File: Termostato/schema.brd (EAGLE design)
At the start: 100 x 80 mm, 5 parts, among them K1 RELAY-SPDT-JZC-11F

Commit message: Updated schematics V1.1
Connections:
- new net 3.3V: B1.3.3V, U$1.B2, U$1.D2
- net RX: now also B1.D2; no longer B1.D3
- net TX: now also B1.D3; no longer B1.D2
- net VCC: no longer U$1.D2
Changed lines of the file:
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@@
 <contactref element="B1" pad="VIN"/>
 <contactref element="U1" pad="VDD"/>
-<contactref element="U$1" pad="D2"/>
-<wire x1="72.39" y1="64.77" x2="85.09" y2="41.91" width="0" layer="19" extent="1-1"/>
 <wire x1="55.88" y1="6.35" x2="85.09" y2="41.91" width="0" layer="19" extent="1-1"/>
 </signal>
@@
 <signal name="TX">
 <contactref element="U$1" pad="A2"/>
-<contactref element="B1" pad="D2"/>
-<wire x1="72.39" y1="72.39" x2="68.58" y2="54.61" width="0" layer="19" extent="1-1"/>
+<contactref element="B1" pad="D3"/>
+<wire x1="72.39" y1="72.39" x2="66.04" y2="54.61" width="0" layer="19" extent="1-1"/>
 </signal>
 <signal name="RX">
 <contactref element="U$1" pad="D1"/>
-<contactref element="B1" pad="D3"/>
-<wire x1="74.93" y1="64.77" x2="66.04" y2="54.61" width="0" layer="19" extent="1-1"/>
+<contactref element="B1" pad="D2"/>
+<wire x1="68.58" y1="54.61" x2="74.93" y2="64.77" width="0" layer="19" extent="1-1"/>
+</signal>
+<signal name="3.3V">
+<contactref element="U$1" pad="D2"/>
+<contactref element="B1" pad="3.3V"/>
+<contactref element="U$1" pad="B2"/>
+<wire x1="72.39" y1="64.77" x2="72.39" y2="69.85" width="0" layer="19" extent="1-1"/>
+<wire x1="45.72" y1="6.35" x2="72.39" y2="64.77" width="0" layer="19" extent="1-1"/>
 </signal>
 </signals>

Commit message: Updated schematic
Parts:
- added LCD1: LCD-16X2SILK, SparkFun-Displays:LCD-16X2
- added R1, R2: 220, SparkFun-Resistors:0603
- added S2, S3: (no value), SparkFun-Retired:TACTILE-PTH
- added VR1: 10k, SparkFun-Resistors:TRIMPOT-SMD-TC33X
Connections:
- new net D10: B1.D10, LCD1.12
- new net D11: B1.D11, LCD1.13
- new net D12: B1.D12, LCD1.14
- new net D13: B1.D13, K1.1
- new net D4: B1.D4, S2.4
- new net D5: B1.D5, S3.4
- new net D8: B1.D8, LCD1.6
- new net D9: B1.D9, LCD1.11
- new net N$1: LCD1.3, VR1.2
- new net N$2: R2.1, S2.3
- new net N$4: R1.1, S3.3
- new net N$5: S3.1
- net D7: now also LCD1.4; no longer K1.1
- net GND: now also LCD1.16, LCD1.2, LCD1.5, R1.2, R2.2, VR1.3
- net VCC: now also LCD1.1, LCD1.15, S2.1, VR1.1
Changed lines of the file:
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@@
 <attribute name="PROD_ID" value="SEN-10167" x="88.9" y="41.91" size="1.778" layer="27" display="off"/>
+</element>
+<element name="LCD1" library="SparkFun-Displays" package="LCD-16X2" value="LCD-16X2SILK" x="57.15" y="26.67">
+<attribute name="SF_ID" value="LCD-00255" x="57.15" y="26.67" size="1.778" layer="27" display="off"/>
+</element>
+<element name="VR1" library="SparkFun-Resistors" package="TRIMPOT-SMD-TC33X" value="10k" x="34.29" y="33.02">
+<attribute name="PROD_ID" value="RES-12428" x="34.29" y="33.02" size="1.778" layer="27" display="off"/>
+</element>
+<element name="S2" library="SparkFun-Retired" package="TACTILE-PTH" value="" x="49.53" y="69.85"/>
+<element name="S3" library="SparkFun-Retired" package="TACTILE-PTH" value="" x="64.77" y="71.12"/>
+<element name="R1" library="SparkFun-Resistors" package="0603" value="220" x="6.35" y="57.15">
+<attribute name="PROD_ID" value="RES-07861" x="6.35" y="57.15" size="1.778" layer="27" display="off"/>
+</element>
+<element name="R2" library="SparkFun-Resistors" package="0603" value="220" x="10.16" y="67.31">
+<attribute name="PROD_ID" value="RES-07861" x="10.16" y="67.31" size="1.778" layer="27" display="off"/>
 </element>
 </elements>
@@
 <contactref element="U1" pad="GND"/>
 <contactref element="U$1" pad="A1"/>
-<wire x1="19.05" y1="62.23" x2="92.71" y2="41.91" width="0" layer="19" extent="1-1"/>
-<wire x1="74.93" y1="72.39" x2="19.05" y2="62.23" width="0" layer="19" extent="1-1"/>
-<wire x1="53.34" y1="6.35" x2="19.05" y2="62.23" width="0" layer="19" extent="1-1"/>
+<contactref element="LCD1" pad="16"/>
+<contactref element="LCD1" pad="2"/>
+<contactref element="LCD1" pad="5"/>
+<contactref element="VR1" pad="3"/>
+<contactref element="R1" pad="2"/>
+<contactref element="R2" pad="2"/>
+<wire x1="7.2" y1="57.15" x2="11.01" y2="67.31" width="0" layer="19" extent="1-1"/>
+<wire x1="35.29" y1="31.195" x2="7.2" y2="57.15" width="0" layer="19" extent="1-1"/>
+<wire x1="35.31" y1="42.17" x2="35.29" y2="31.195" width="0" layer="19" extent="1-1"/>
+<wire x1="27.69" y1="42.17" x2="35.31" y2="42.17" width="0" layer="19" extent="1-1"/>
+<wire x1="19.05" y1="62.23" x2="27.69" y2="42.17" width="0" layer="19" extent="1-1"/>
+<wire x1="63.25" y1="42.17" x2="35.31" y2="42.17" width="0" layer="19" extent="1-1"/>
+<wire x1="92.71" y1="41.91" x2="63.25" y2="42.17" width="0" layer="19" extent="1-1"/>
+<wire x1="53.34" y1="6.35" x2="35.29" y2="31.195" width="0" layer="19" extent="1-1"/>
+<wire x1="74.93" y1="72.39" x2="63.25" y2="42.17" width="0" layer="19" extent="1-1"/>
 </signal>
 <signal name="VCC">
 <contactref element="B1" pad="VIN"/>
 <contactref element="U1" pad="VDD"/>
-<wire x1="55.88" y1="6.35" x2="85.09" y2="41.91" width="0" layer="19" extent="1-1"/>
+<contactref element="LCD1" pad="1"/>
+<contactref element="VR1" pad="1"/>
+<contactref element="LCD1" pad="15"/>
+<contactref element="S2" pad="1"/>
+<wire x1="60.71" y1="42.17" x2="85.09" y2="41.91" width="0" layer="19" extent="1-1"/>
+<wire x1="33.29" y1="31.195" x2="60.71" y2="42.17" width="0" layer="19" extent="1-1"/>
+<wire x1="25.15" y1="42.17" x2="33.29" y2="31.195" width="0" layer="19" extent="1-1"/>
+<wire x1="55.88" y1="6.35" x2="33.29" y2="31.195" width="0" layer="19" extent="1-1"/>
+<wire x1="46.2788" y1="72.1106" x2="25.15" y2="42.17" width="0" layer="19" extent="1-1"/>
 </signal>
 <signal name="N$3">
@@
 </signal>
 <signal name="D7">
-<contactref element="K1" pad="1"/>
 <contactref element="B1" pad="D7"/>
-<wire x1="55.88" y1="54.61" x2="26.67" y2="62.23" width="0" layer="19" extent="1-1"/>
+<contactref element="LCD1" pad="4"/>
+<wire x1="32.77" y1="42.17" x2="55.88" y2="54.61" width="0" layer="19" extent="1-1"/>
 </signal>
 <signal name="TX">
@@
 <wire x1="45.72" y1="6.35" x2="72.39" y2="64.77" width="0" layer="19" extent="1-1"/>
 </signal>
+<signal name="N$1">
+<contactref element="LCD1" pad="3"/>
+<contactref element="VR1" pad="2"/>
+<wire x1="30.23" y1="42.17" x2="34.29" y2="34.52" width="0" layer="19" extent="1-1"/>
+</signal>
+<signal name="D13">
+<contactref element="K1" pad="1"/>
+<contactref element="B1" pad="D13"/>
+<wire x1="26.67" y1="62.23" x2="39.116" y2="54.61" width="0" layer="19" extent="1-1"/>
+</signal>
+<signal name="D8">
+<contactref element="LCD1" pad="6"/>
+<contactref element="B1" pad="D8"/>
+<wire x1="37.85" y1="42.17" x2="51.816" y2="54.61" width="0" layer="19" extent="1-1"/>
+</signal>
+<signal name="D9">
+<contactref element="LCD1" pad="11"/>
+<contactref element="B1" pad="D9"/>
+<wire x1="50.55" y1="42.17" x2="49.276" y2="54.61" width="0" layer="19" extent="1-1"/>
+</signal>
+<signal name="D10">
+<contactref element="LCD1" pad="12"/>
+<contactref element="B1" pad="D10"/>
+<wire x1="53.09" y1="42.17" x2="46.736" y2="54.61" width="0" layer="19" extent="1-1"/>
+</signal>
+<signal name="D11">
+<contactref element="LCD1" pad="13"/>
+<contactref element="B1" pad="D11"/>
+<wire x1="55.63" y1="42.17" x2="44.196" y2="54.61" width="0" layer="19" extent="1-1"/>
+</signal>
+<signal name="D12">
+<contactref element="LCD1" pad="14"/>
+<contactref element="B1" pad="D12"/>
+<wire x1="41.656" y1="54.61" x2="58.17" y2="42.17" width="0" layer="19" extent="1-1"/>
+</signal>
+<signal name="N$2">
+<contactref element="R2" pad="1"/>
+<contactref element="S2" pad="3"/>
+<wire x1="46.2788" y1="67.5894" x2="9.31" y2="67.31" width="0" layer="19" extent="1-1"/>
+</signal>
+<signal name="N$4">
+<contactref element="R1" pad="1"/>
+<contactref element="S3" pad="3"/>
+<wire x1="61.5188" y1="68.8594" x2="5.5" y2="57.15" width="0" layer="19" extent="1-1"/>
+</signal>
+<signal name="N$5">
+<contactref element="S3" pad="1"/>
+</signal>
+<signal name="D4">
+<contactref element="S2" pad="4"/>
+<contactref element="B1" pad="D4"/>
+<wire x1="63.5" y1="54.61" x2="52.7812" y2="67.5894" width="0" layer="19" extent="1-1"/>
+</signal>
+<signal name="D5">
+<contactref element="S3" pad="4"/>
+<contactref element="B1" pad="D5"/>
+<wire x1="60.96" y1="54.61" x2="68.0212" y2="68.8594" width="0" layer="19" extent="1-1"/>
+</signal>
 </signals>

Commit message: Updated scematic
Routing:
- net GND: track 0.00 -> 179.7 mm
- net VCC: track 0.00 -> 135.4 mm
- net 3.3V: track 0.00 -> 75.4 mm
- net N$4: track 0.00 -> 60.9 mm
- net N$2: track 0.00 -> 37.8 mm
- net N$3: track 0.00 -> 34.5 mm
- net D7: track 0.00 -> 29.9 mm
- net D12: track 0.00 -> 28.4 mm
- net D11: track 0.00 -> 24.1 mm
- net D8: track 0.00 -> 22.0 mm
- net TX: track 0.00 -> 20.4 mm
- net D4: track 0.00 -> 17.4 mm
- net D5: track 0.00 -> 17.2 mm
- net D13: track 0.00 -> 15.6 mm
- net D10: track 0.00 -> 15.1 mm
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
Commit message: Arduino shield
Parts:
- B1: value ARDUINO_UNO_R3NO_HOLES -> ARDUINO_UNO_R3_SHIELDBASIC; device SparkFun-Boards:ARDUINO_R3_NO_HOLES -> SparkFun-Boards:UNO_R3_SHIELD
- moved K1 60.8 mm to (49.5, 16.5), turned to 90 degrees
- moved U$1 57.0 mm to (95.2, 12.7)
- moved VR1 44.5 mm to (78.7, 30.5), turned to 180 degrees
- moved R2 44.1 mm to (39.4, 34.3)
- moved S2 41.9 mm to (50.8, 27.9)
- moved R1 36.4 mm to (39.4, 41.9), turned to 180 degrees
- moved S3 35.4 mm to (52.1, 38.1)
- moved U1 34.9 mm to (69.8, 12.7), turned to 180 degrees
- moved LCD1 34.4 mm to (59.7, 61.0), turned to 180 degrees
- moved B1 21.9 mm to (66.0, 26.7), turned to 270 degrees
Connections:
- net 3.3V: no longer B1.3.3V
- net GND: now also B1.GND@0; no longer B1.GND@2
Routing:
- net 3.3V: track 75.4 -> 5.96 mm
- net N$4: track 60.9 -> 11.1 mm
- net GND: track 179.7 -> 139.8 mm
- net VCC: track 135.4 -> 104.0 mm
- net RX: track 12.8 -> 43.1 mm
- net D4: track 17.4 -> 46.7 mm
- net N$2: track 37.8 -> 12.6 mm
- net D12: track 28.4 -> 5.78 mm
- net D13: track 15.6 -> 35.4 mm
- net D11: track 24.1 -> 5.75 mm
- net D7: track 29.9 -> 12.6 mm
- net TX: track 20.4 -> 35.2 mm
- net D5: track 17.2 -> 30.2 mm
- net N$3: track 34.5 -> 46.8 mm
- net D8: track 22.0 -> 11.4 mm
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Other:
- outline, holes or cut-outs redrawn

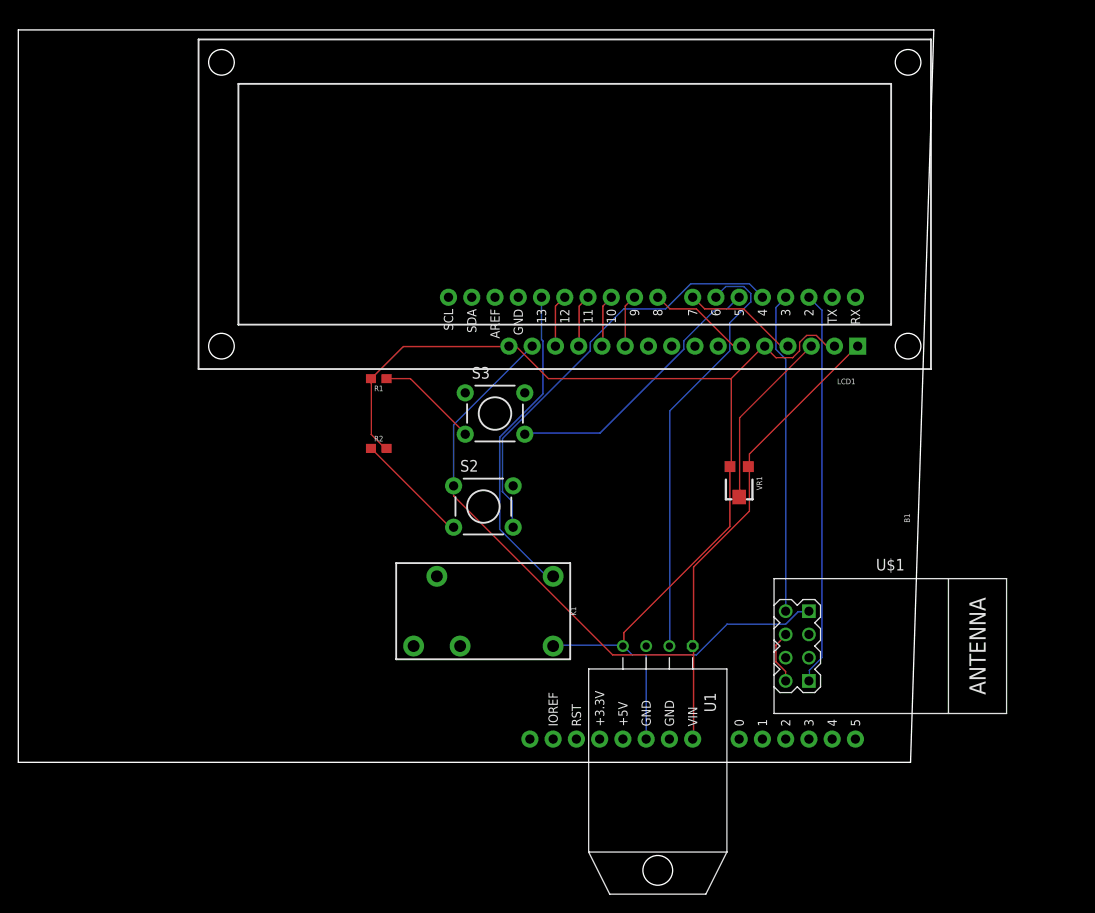
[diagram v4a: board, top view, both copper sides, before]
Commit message: Update schematics: add 3.3V connection and switch from VIN to 5V
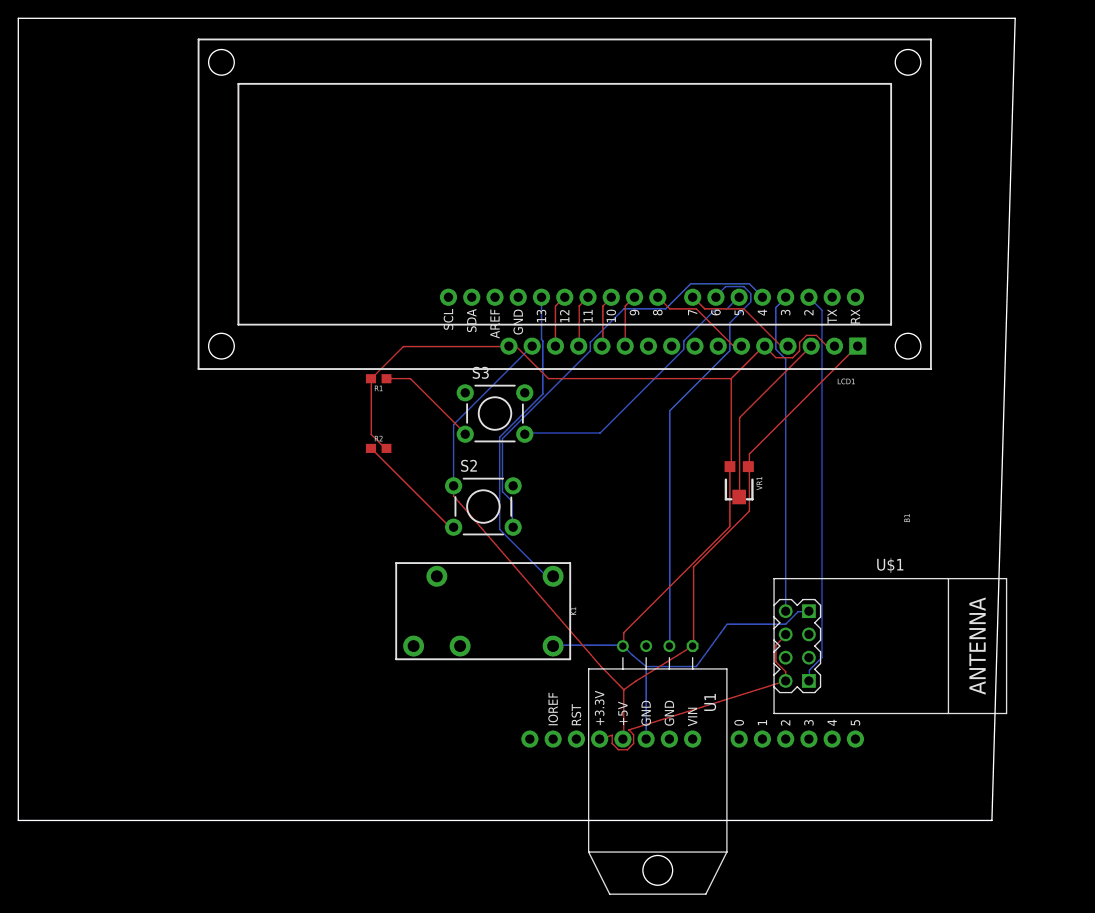
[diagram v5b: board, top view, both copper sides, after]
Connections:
- net 3.3V: now also B1.3.3V
- net VCC: now also B1.5V; no longer B1.VIN
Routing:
- net 3.3V: track 5.96 -> 30.9 mm
- net VCC: track 104.0 -> 102.7 mm
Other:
- board size 100 x 80 mm -> 108.9 x 87.6 mm
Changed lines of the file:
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@@
 <board>
 <plain>
-<wire x1="0" y1="0" x2="97.46" y2="0" width="0" layer="20"/>
-<wire x1="97.46" y1="0" x2="100" y2="80" width="0" layer="20"/>
-<wire x1="100" y1="80" x2="0" y2="80" width="0" layer="20"/>
-<wire x1="0" y1="80" x2="0" y2="0" width="0" layer="20"/>
+<wire x1="0" y1="-6.35" x2="106.35" y2="-6.35" width="0" layer="20"/>
+<wire x1="106.35" y1="-6.35" x2="108.89" y2="81.27" width="0" layer="20"/>
+<wire x1="108.89" y1="81.27" x2="0" y2="81.27" width="0" layer="20"/>
+<wire x1="0" y1="81.27" x2="0" y2="-6.35" width="0" layer="20"/>
 </plain>
 <attributes>
@@
 <wire x1="83.82" y1="15.0876" x2="85.1916" y2="16.4592" width="0.1524" layer="16"/>
 <wire x1="77.4192" y1="15.0876" x2="83.82" y2="15.0876" width="0.1524" layer="16"/>
-<wire x1="74.0664" y1="11.7348" x2="77.4192" y2="15.0876" width="0.1524" layer="16"/>
-<wire x1="67.056" y1="11.7348" x2="68.58" y2="11.7348" width="0.1524" layer="16"/>
-<wire x1="68.58" y1="11.7348" x2="74.0664" y2="11.7348" width="0.1524" layer="16"/>
+<wire x1="74.0664" y1="10.4648" x2="77.4192" y2="15.0876" width="0.1524" layer="16"/>
+<wire x1="67.056" y1="11.7348" x2="68.58" y2="10.4648" width="0.1524" layer="16"/>
+<wire x1="68.58" y1="10.4648" x2="74.0664" y2="10.4648" width="0.1524" layer="16"/>
 <wire x1="66.1416" y1="12.6492" x2="67.056" y2="11.7348" width="0.1524" layer="16"/>
 <wire x1="86.2584" y1="16.4592" x2="86.36" y2="16.51" width="0.1524" layer="16"/>
 <wire x1="66.1416" y1="12.6492" x2="66.04" y2="12.7" width="0.1524" layer="16"/>
-<wire x1="68.58" y1="11.7348" x2="68.58" y2="2.54" width="0.1524" layer="16"/>
+<wire x1="68.58" y1="10.4648" x2="68.58" y2="2.54" width="0.1524" layer="16"/>
 <wire x1="77.724" y1="25.7556" x2="77.724" y2="32.1564" width="0.1524" layer="1"/>
 <wire x1="66.1416" y1="14.1732" x2="77.724" y2="25.7556" width="0.1524" layer="1"/>
@@
 <contactref element="LCD1" pad="15"/>
 <contactref element="S2" pad="1"/>
-<contactref element="B1" pad="VIN"/>
 <wire x1="47.5488" y1="36.8808" x2="47.5488" y2="30.2006" width="0.1524" layer="16"/>
 <wire x1="56.0832" y1="45.4152" x2="47.5488" y2="36.8808" width="0.1524" layer="16"/>
 <wire x1="56.0832" y1="45.4152" x2="56.13" y2="45.46" width="0.1524" layer="16"/>
-<wire x1="73.7616" y1="2.5908" x2="73.7616" y2="11.7348" width="0.1524" layer="1"/>
-<wire x1="73.7616" y1="11.7348" x2="73.7616" y2="12.6492" width="0.1524" layer="1"/>
-<wire x1="73.7616" y1="12.6492" x2="73.66" y2="12.7" width="0.1524" layer="1"/>
-<wire x1="73.7616" y1="2.5908" x2="73.66" y2="2.54" width="0.1524" layer="1"/>
+<wire x1="66.1416" y1="2.5908" x2="66.1416" y2="7.9248" width="0.1524" layer="1"/>
+<wire x1="66.1416" y1="7.9248" x2="67.4116" y2="8.8392" width="0.1524" layer="1"/>
+<wire x1="67.4116" y1="8.8392" x2="73.66" y2="12.7" width="0.1524" layer="1"/>
 <wire x1="79.8576" y1="33.6804" x2="79.8576" y2="32.3088" width="0.1524" layer="1"/>
 <wire x1="91.5924" y1="45.4152" x2="79.8576" y2="33.6804" width="0.1524" layer="1"/>
@@
 <wire x1="79.8576" y1="32.1564" x2="79.74" y2="32.305" width="0.1524" layer="1"/>
 <wire x1="47.5488" y1="29.1084" x2="47.5488" y2="30.2006" width="0.1524" layer="1"/>
-<wire x1="64.9224" y1="11.7348" x2="47.5488" y2="29.1084" width="0.1524" layer="1"/>
-<wire x1="73.7616" y1="11.7348" x2="64.9224" y2="11.7348" width="0.1524" layer="1"/>
+<wire x1="63.6524" y1="10.4648" x2="47.5488" y2="29.1084" width="0.1524" layer="1"/>
+<wire x1="66.1416" y1="7.9248" x2="63.6524" y2="10.4648" width="0.1524" layer="1"/>
+<contactref element="B1" pad="5V"/>
+<wire x1="66.04" y1="2.54" x2="66.1416" y2="2.5908" width="0" layer="19" extent="1-1"/>
 </signal>
 <signal name="N$3">
@@
 <contactref element="U$1" pad="D2"/>
 <contactref element="U$1" pad="B2"/>
-<wire x1="83.82" y1="9.906" x2="83.82" y2="8.89" width="0.1524" layer="1"/>
+<wire x1="83.82" y1="8.89" x2="83.82" y2="9.906" width="0.1524" layer="1"/>
 <wire x1="82.7532" y1="10.9728" x2="83.82" y2="9.906" width="0.1524" layer="1"/>
 <wire x1="82.7532" y1="12.8016" x2="82.7532" y2="10.9728" width="0.1524" layer="1"/>
 <wire x1="83.82" y1="13.8684" x2="82.7532" y2="12.8016" width="0.1524" layer="1"/>
 <wire x1="83.82" y1="13.8684" x2="83.82" y2="13.97" width="0.1524" layer="1"/>
+<contactref element="B1" pad="3.3V"/>
+<wire x1="63.5" y1="2.54" x2="64.8716" y2="2.968625" width="0.1524" layer="1"/>
+<wire x1="64.8716" y1="2.968625" x2="64.8716" y2="2.05603125" width="0.1524" layer="1"/>
+<wire x1="64.8716" y1="2.05603125" x2="65.55603125" y2="1.3716" width="0.1524" layer="1"/>
+<wire x1="65.55603125" y1="1.3716" x2="66.52396875" y2="1.3716" width="0.1524" layer="1"/>
+<wire x1="66.52396875" y1="1.3716" x2="67.2084" y2="2.05603125" width="0.1524" layer="1"/>
+<wire x1="67.2084" y1="2.05603125" x2="67.2084" y2="3.02396875" width="0.1524" layer="1"/>
+<wire x1="67.2084" y1="3.02396875" x2="66.694184375" y2="3.538184375" width="0.1524" layer="1"/>
+<wire x1="66.694184375" y1="3.538184375" x2="83.82" y2="8.89" width="0.1524" layer="1"/>
 </signal>
 <signal name="N$1">

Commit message: Updated board design
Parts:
- removed R1, R2: 220, SparkFun-Resistors:0603
- removed VR1: 10k, SparkFun-Resistors:TRIMPOT-SMD-TC33X
- added R3, R4: 220, resistor:0204/7
- moved S3 38.9 mm to (82.5, 14.0), turned to 180 degrees
- moved S2 31.8 mm to (82.5, 26.7), turned to 90 degrees
- moved U$1 27.7 mm to (102.9, 39.4)
- moved U1 18.0 mm to (67.3, 30.5), turned to 0 degrees
- moved LCD1 15.3 mm to (45.7, 54.6)
- moved K1 4.58 mm to (45.7, 19.1)
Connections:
- removed net N$1: LCD1.3, VR1.2
- net GND: now also R3.2, R4.2; no longer R1.2, R2.2, VR1.3
- net N$2: now also R3.1; no longer R2.1
- net N$4: now also R4.1; no longer R1.1
- net VCC: no longer VR1.1
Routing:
- net GND: track 139.9 -> 0.00 mm
- net VCC: track 102.7 -> 0.00 mm
- net 3.3V: track 30.9 -> 77.3 mm
- net D13: track 35.4 -> 63.5 mm
- net TX: track 35.2 -> 11.7 mm
- net D4: track 46.7 -> 24.8 mm
- net D11: track 5.75 -> 26.7 mm
- net D10: track 5.76 -> 26.7 mm
- net D9: track 5.78 -> 26.7 mm
- net D12: track 5.78 -> 26.7 mm
- net N$1: track 19.7 -> 0.00 mm
- net D5: track 30.2 -> 47.8 mm
- net RX: track 43.1 -> 27.2 mm
- net N$3: track 46.8 -> 38.1 mm
- net N$4: track 11.1 -> 3.32 mm
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- added copper zone on layer 16, net GND
- added copper zone on layer 1, net VCC
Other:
- board size 108.9 x 87.6 mm -> 59.4 x 53.3 mm
